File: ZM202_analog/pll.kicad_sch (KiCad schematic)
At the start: 29 parts, among them U13 LM393B, U14 LM358B, U3 LM348B

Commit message: Connected hierarchical outlets to connector.
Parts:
- added C16, C17, C18: C0603_100nF_25V, Capacitor_SMD:C_0603_1608Metric, symbol Jojos_Lib:C0603_100nF_25V
- added unit 4 of U12
- added unit 4 of U13
- added U15: CD4027, Package_SO:SO-16_3.9x9.9mm_P1.27mm, symbol Jojos_Lib:CD4027BM96
- added unit 3 of U16
- added unit 3 of U17
- gave numbers to parts that had none: 1
- renumbered C15 to C11, C9 to C12, C14 to C13, C13 to C14, C11 to C15, R47 to R38, R42 to R39, R46 to R40, R43 to R42, R48 to R43, R49 to R44, R39 to R45, R40 to R46, R50 to R47, R38 to R48, R45 to R49, R52 to R50, U15 to U13, U17 to U14, U13 to U16, U14 to U17, U16 to U18
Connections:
- net +5V: now also C16.2, C17.2, C18.2, U12.16 (VDD), U13.16 (VDD), U15.16 (+), U16.8 (+), U17.8 (+)
- net GND: now also C16.1, U12.6 (INH), U12.8 (VSS), U13.6 (INH), U13.8 (VSS), U15.8 (-)
- new net -5V: C17.1, C18.1, U12.7 (VEE), U13.7 (VEE), U16.4 (-), U17.4 (-)
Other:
- moved on the sheet: C13, C14, R38, R40, R42, R43, R44, R47, R48, R50, R51, U12A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

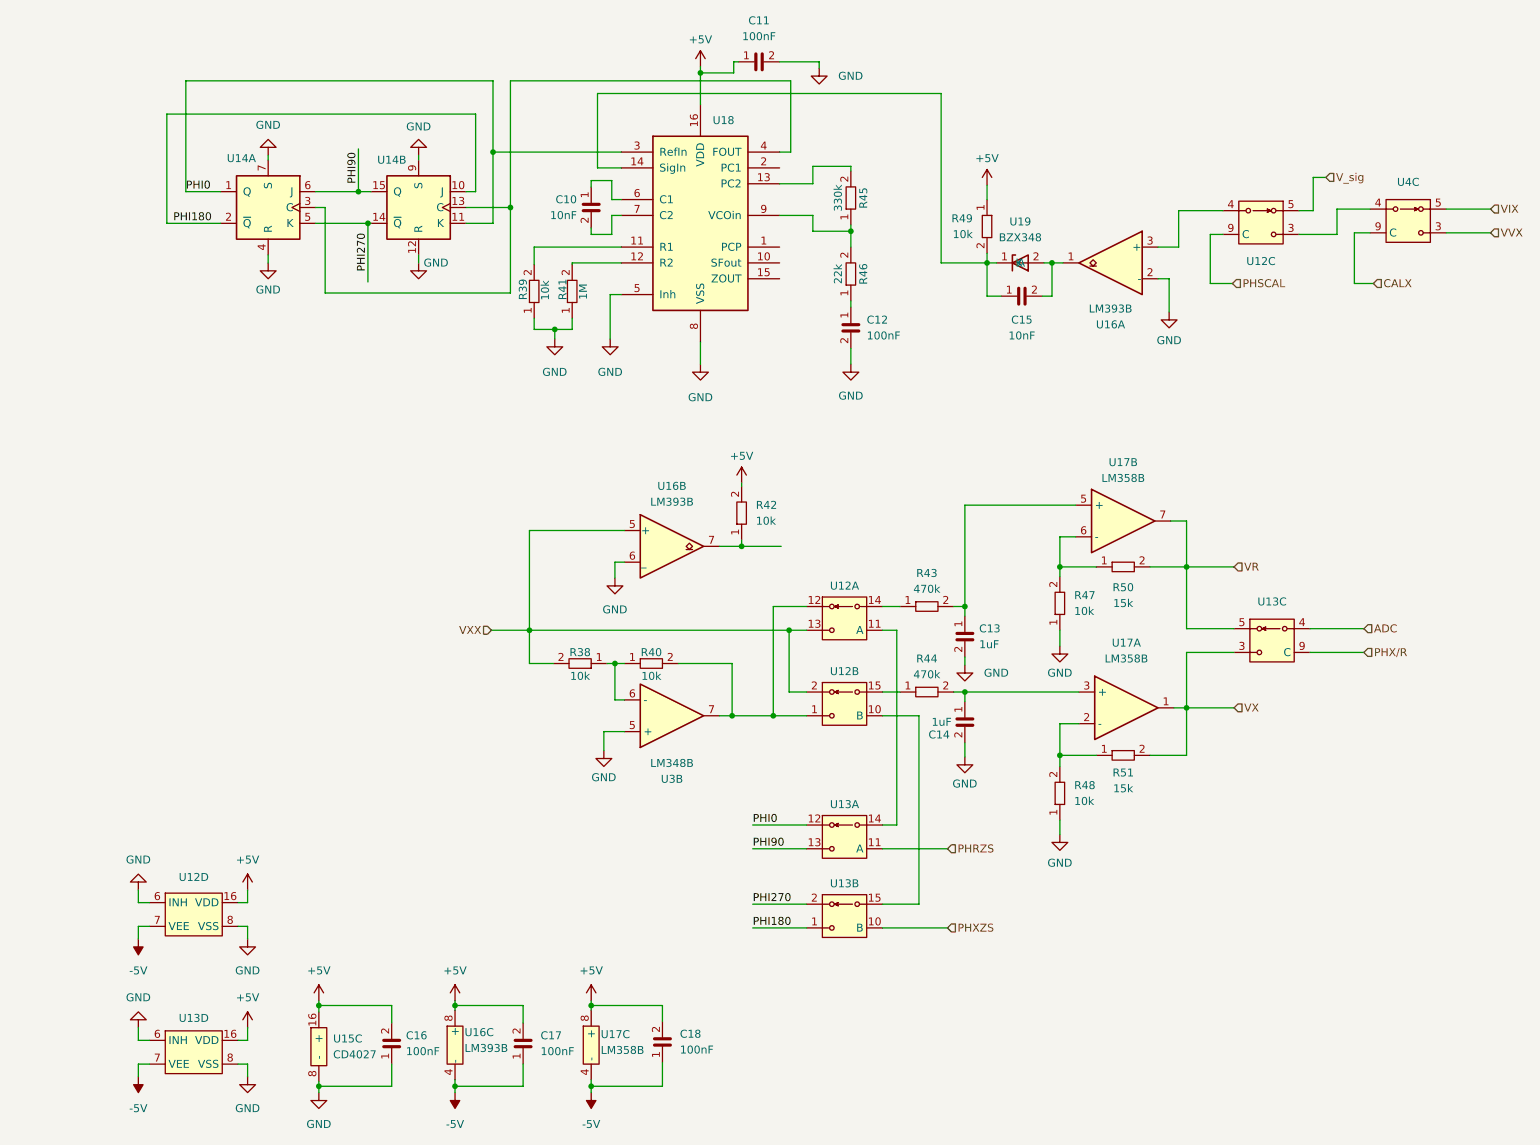
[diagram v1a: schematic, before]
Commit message: Changed amplification resistor/cap in the analog core to 82nF/2.49k and did some various changes in the symbols and updated them into the schematic. Added PWR-flags
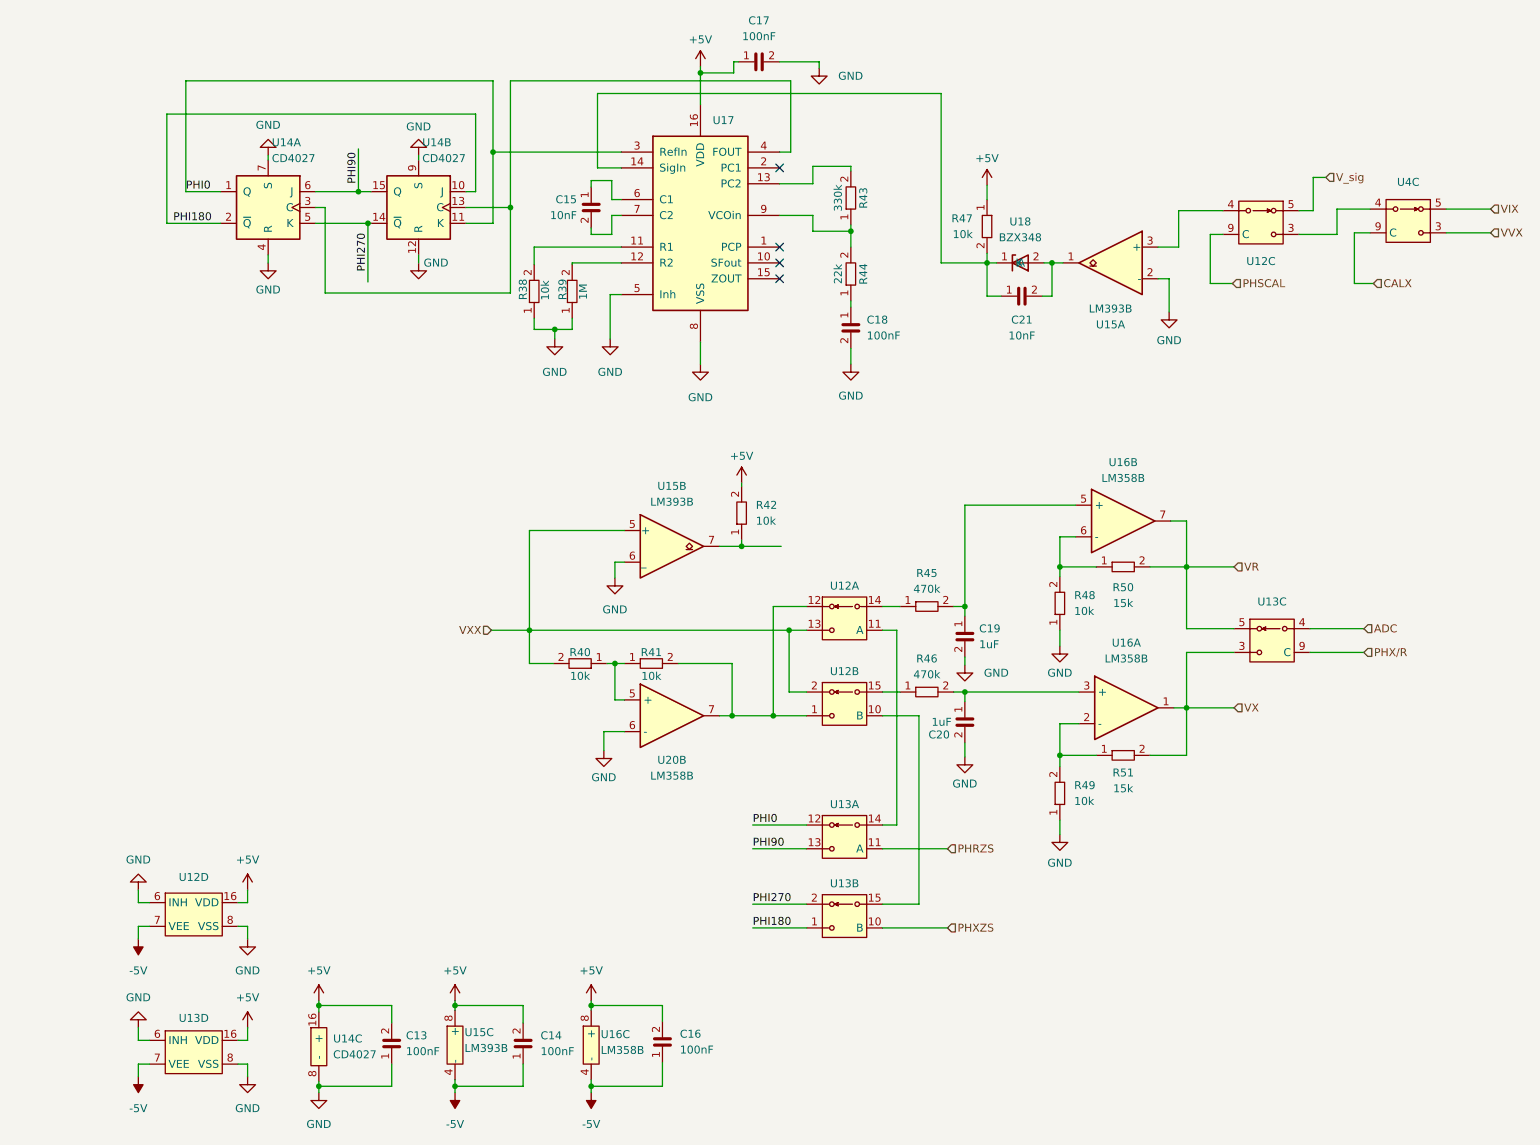
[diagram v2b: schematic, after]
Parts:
- removed U3: LM348B, Package_SO:SO-8_3.9x4.9mm_P1.27mm, symbol Jojos_Lib:LM348B
- added U20: LM358B, Package_SO:SO-8_3.9x4.9mm_P1.27mm, symbol Jojos_Lib:LM358B
- U14: value ~ -> CD4027
- renumbered C16 to C13, C17 to C14, C10 to C15, C18 to C16, C11 to C17, C12 to C18, C13 to C19, C14 to C20, C15 to C21, R39 to R38, R41 to R39, R38 to R40, R40 to R41, R45 to R43, R46 to R44, R43 to R45, R44 to R46, R49 to R47, R47 to R48, R48 to R49, U15 to U14, U16 to U15, U17 to U16, U18 to U17, U19 to U18
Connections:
- net GND: now also U20.6 (-)
- net at R41.2, U12.1, U12.12: now also U20.7
- net at R40.1, R41.1: now also U20.5 (+)
- no-connect marks 0 -> 4

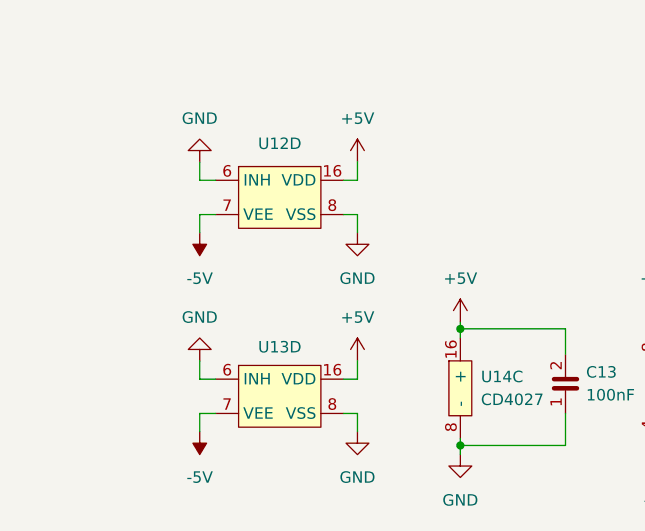
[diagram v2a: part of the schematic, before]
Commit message: Finished first version of PCB. Added some capacitors at digital ICs.
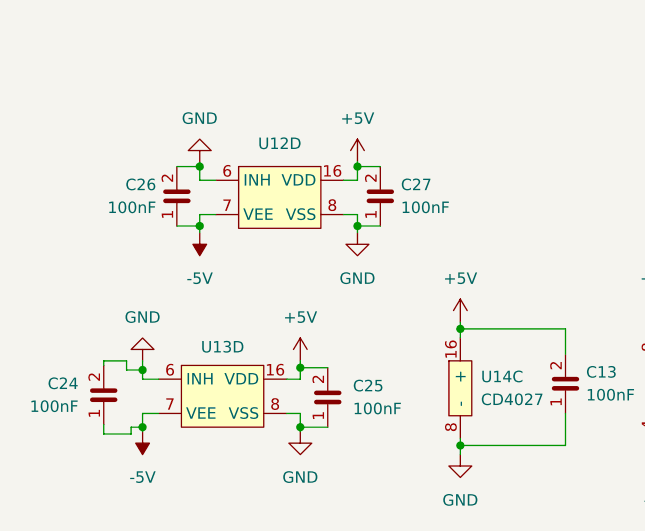
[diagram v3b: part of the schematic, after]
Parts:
- added C24, C25, C26, C27: C0603_100nF_25V, Capacitor_SMD:C_0603_1608Metric, symbol Jojos_Lib:C0603_100nF_25V
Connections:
- net +5V: now also C25.2, C27.2
- net -5V: now also C24.1, C26.1
- net GND: now also C24.2, C25.1, C26.2, C27.1
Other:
- moved on the sheet: U13D
